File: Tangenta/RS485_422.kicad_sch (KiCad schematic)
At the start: 39 parts, among them Q3 BSS138, U19 SN75HVD3082EDR, U20 SN75HVD3082EDR, U21 TPCDSOT23-SM712, U22 TPCDSOT23-SM712

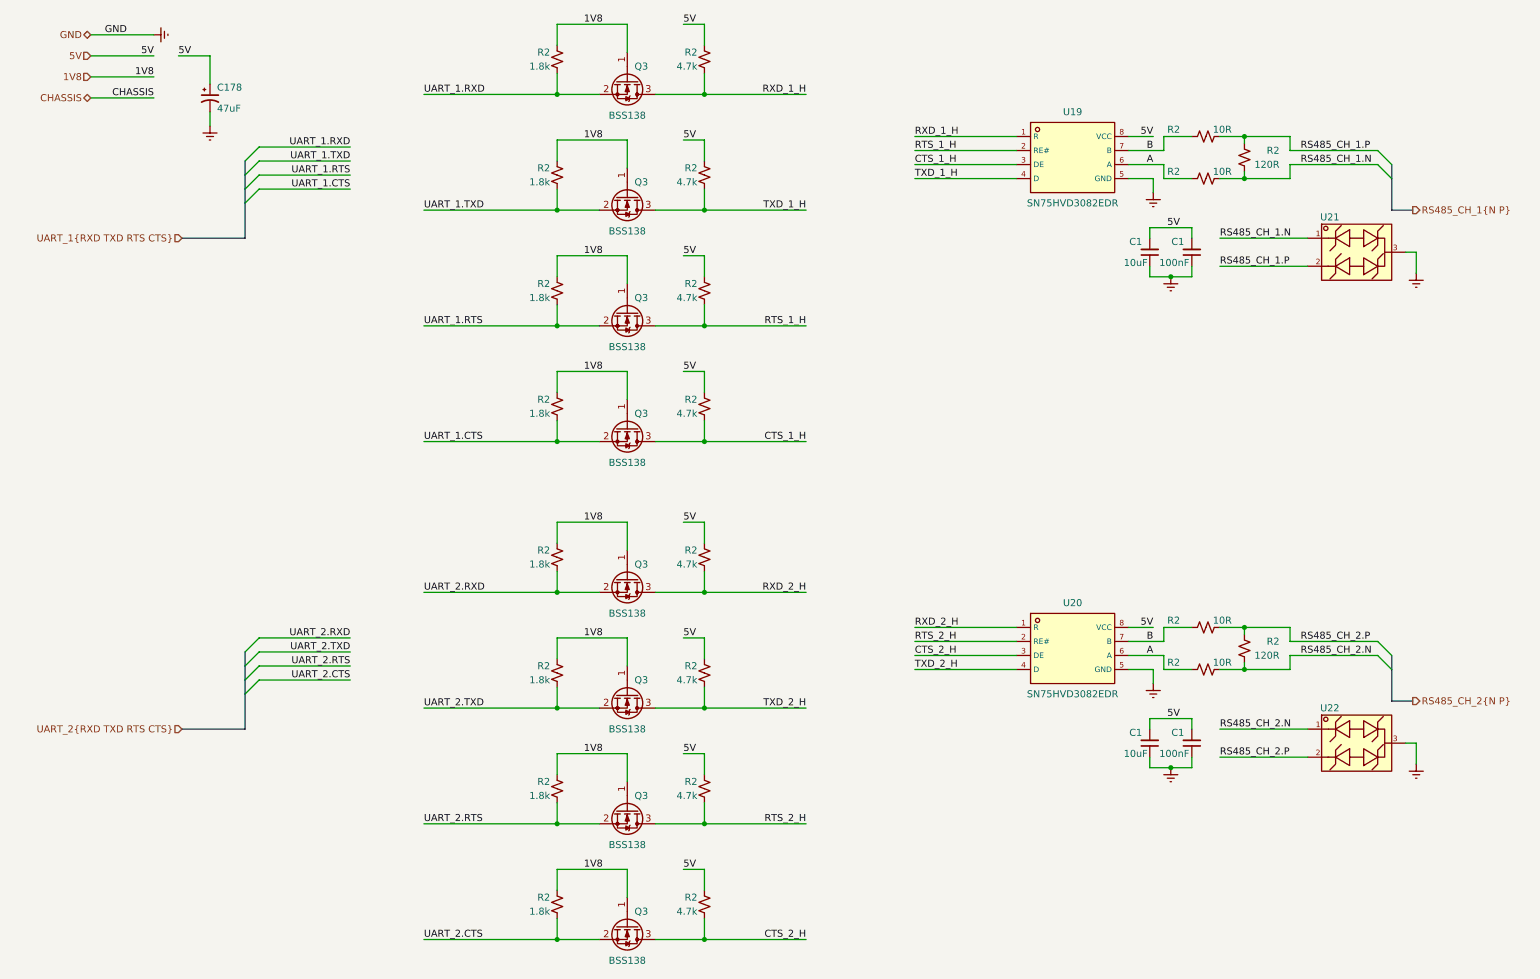
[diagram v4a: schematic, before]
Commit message: Removing the old RS485 non-isolated transceivers.
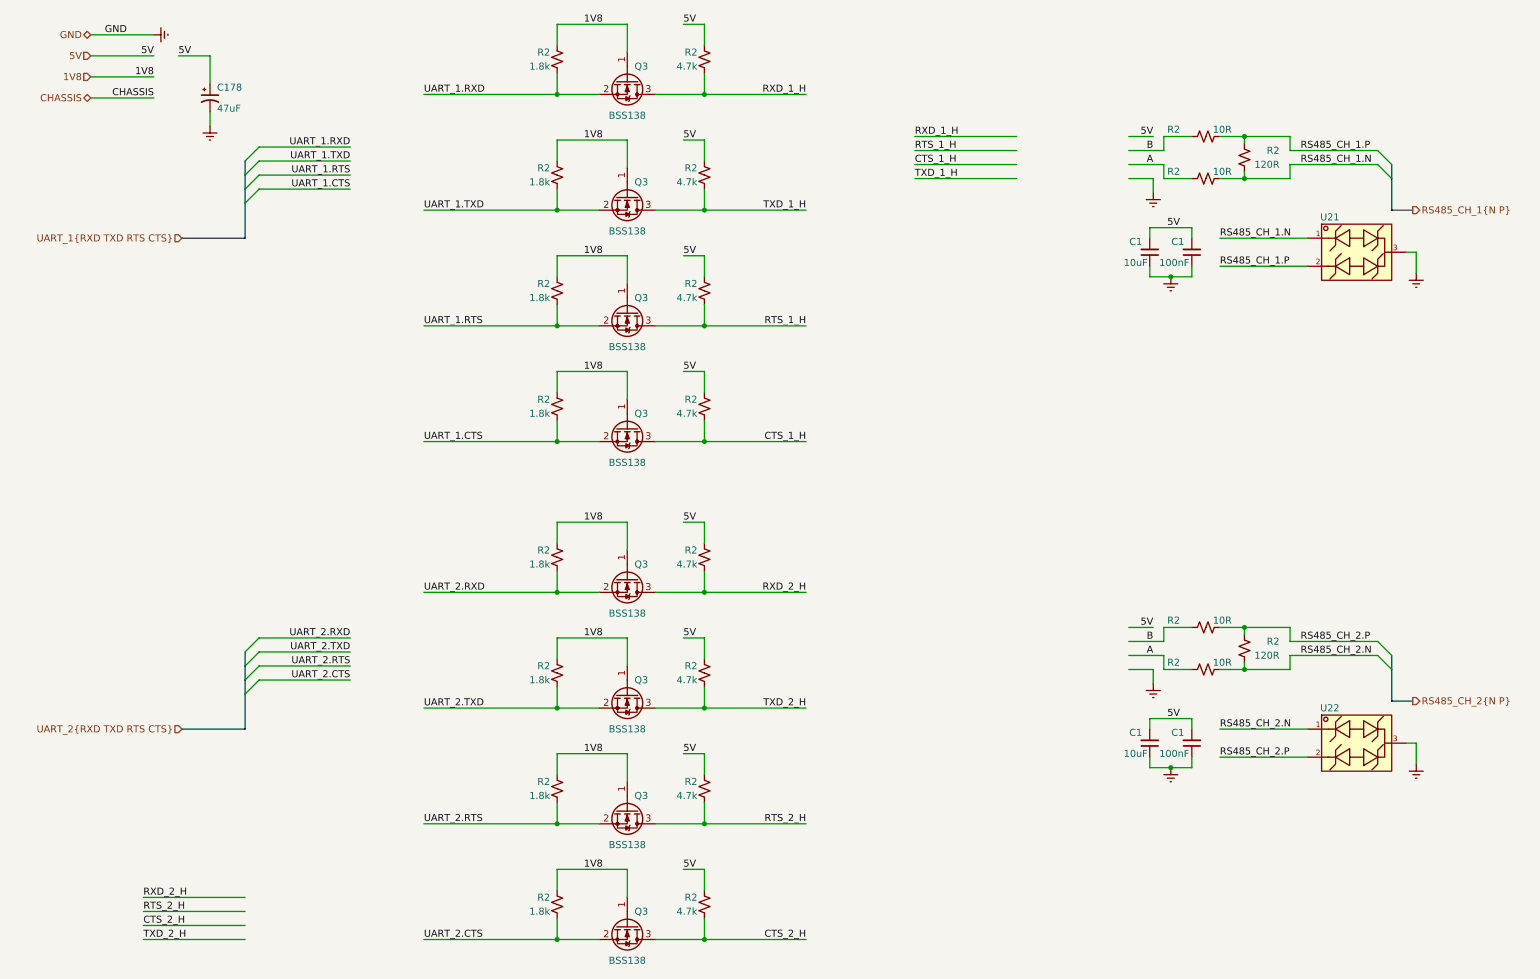
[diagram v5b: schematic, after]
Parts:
- removed U19, U20: SN75HVD3082EDR, RS485_TRANS:RS485_TRANS, symbol RS485_TRANS:SN75HVD3082EDR
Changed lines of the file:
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@@
     (stroke (width 0) (type default))
   )
-  (wire (pts (xy 175.895 138.43) (xy 194.31 138.43))
+  (wire (pts (xy 36.195 187.325) (xy 54.61 187.325))
     (stroke (width 0) (type default))
   )
@@
     (stroke (width 0) (type default))
   )
-  (wire (pts (xy 194.31 130.81) (xy 175.895 130.81))
+  (wire (pts (xy 54.61 179.705) (xy 36.195 179.705))
     (stroke (width 0) (type default))
   )
@@
     (stroke (width 0) (type default))
   )
-  (wire (pts (xy 175.895 133.35) (xy 194.31 133.35))
+  (wire (pts (xy 36.195 182.245) (xy 54.61 182.245))
     (stroke (width 0) (type default))
   )
@@
     (stroke (width 0) (type default))
   )
-  (wire (pts (xy 175.895 135.89) (xy 194.31 135.89))
+  (wire (pts (xy 36.195 184.785) (xy 54.61 184.785))
     (stroke (width 0) (type default))
   )
@@
     (effects (font (size 1.27 1.27)) (justify left bottom))
   )
-  (label "RTS_2_H" (at 175.895 133.35 0) (fields_autoplaced)
+  (label "RTS_2_H" (at 36.195 182.245 0) (fields_autoplaced)
     (effects (font (size 1.27 1.27)) (justify left bottom))
   )
@@
     (effects (font (size 1.27 1.27)) (justify left bottom))
   )
-  (label "TXD_2_H" (at 175.895 138.43 0) (fields_autoplaced)
+  (label "TXD_2_H" (at 36.195 187.325 0) (fields_autoplaced)
     (effects (font (size 1.27 1.27)) (justify left bottom))
   )
@@
     (effects (font (size 1.27 1.27)) (justify right bottom))
   )
-  (label "RXD_2_H" (at 175.895 130.81 0) (fields_autoplaced)
+  (label "RXD_2_H" (at 36.195 179.705 0) (fields_autoplaced)
     (effects (font (size 1.27 1.27)) (justify left bottom))
   )
@@
     (effects (font (size 1.27 1.27)) (justify right bottom))
   )
-  (label "CTS_2_H" (at 175.895 135.89 0) (fields_autoplaced)
+  (label "CTS_2_H" (at 36.195 184.785 0) (fields_autoplaced)
     (effects (font (size 1.27 1.27)) (justify left bottom))
   )
@@
     )
   )
-  (symbol (lib_id "RS485_TRANS:SN75HVD3082EDR") (at 204.47 134.62 0) (unit 1)
-    (in_bom yes) (on_board yes) (dnp no)
-    (property "Reference" "U20" (at 204.47 126.365 0)
-      (effects (font (size 1.27 1.27)))
-    )
-    (property "Value" "SN75HVD3082EDR" (at 204.47 142.875 0)
-      (effects (font (size 1.27 1.27)))
-    )
-    (property "Footprint" "RS485_TRANS:RS485_TRANS" (at 208.788 147.955 0)
-      (effects (font (size 1.27 1.27) italic) hide)
-    )
-    (property "Datasheet" "https://so.szlcsc.com/global.html?c=&k=C9843" (at 195.58 150.241 0)
-      (effects (font (size 1.27 1.27)) (justify left) hide)
-    )
-    (property "LCSC" "C140254" (at 199.898 145.796 0)
-      (effects (font (size 1.27 1.27)) hide)
-    )
-    (pin "1")
-    (pin "2")
-    (pin "3")
-    (pin "4")
-    (pin "5")
-    (pin "6")
-    (pin "7")
-    (pin "8")
-    (instances
-      (project "Tangenta"
-        (path "/358d1bcf-7599-4352-8c4d-baa18a5f09e6/98e3b24f-9927-4339-b8fd-9deea91a522a"
-          (reference "U20") (unit 1)
-        )
-      )
-    )
-  )
   (symbol (lib_id "Device:R_Small_US") (at 137.795 27.94 180) (unit 1)
     (in_bom yes) (on_board yes) (dnp no)
@@
         )
       )
-    )
-  )
-  (symbol (lib_id "RS485_TRANS:SN75HVD3082EDR") (at 204.47 45.72 0) (unit 1)
-    (in_bom yes) (on_board yes) (dnp no)
-    (property "Reference" "U19" (at 204.47 37.465 0)
-      (effects (font (size 1.27 1.27)))
-    )
-    (property "Value" "SN75HVD3082EDR" (at 204.47 53.975 0)
-      (effects (font (size 1.27 1.27)))
-    )
-    (property "Footprint" "RS485_TRANS:RS485_TRANS" (at 208.788 59.055 0)
-      (effects (font (size 1.27 1.27) italic) hide)
-    )
-    (property "Datasheet" "https://so.szlcsc.com/global.html?c=&k=C9843" (at 195.58 61.341 0)
-      (effects (font (size 1.27 1.27)) (justify left) hide)
-    )
-    (property "LCSC" "C140254" (at 199.898 56.896 0)
-      (effects (font (size 1.27 1.27)) hide)
-    )
-    (pin "1")
-    (pin "2")
-    (pin "3")
-    (pin "4")
-    (pin "5")
-    (pin "6")
-    (pin "7")
-    (pin "8")
-    (instances
-      (project "Tangenta"
-        (path "/358d1bcf-7599-4352-8c4d-baa18a5f09e6/98e3b24f-9927-4339-b8fd-9deea91a522a"
-          (reference "U19") (unit 1)
-        )
-      )
